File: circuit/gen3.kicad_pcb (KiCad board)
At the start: 2 copper layers, 100 x 88.9 mm, 43 parts, among them J1 Jack-DC, J2 Conn_02x20_Row_Letter_Last, J3 Conn_02x20_Row_Letter_Last, J4 Conn_01x02_Socket, Q1 2SC1815, Q2 2SC1815, Q3 2SC1815, Q4 2SC1815, Q5 2SC1815, SW1 SW_Wuerth_450301014042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

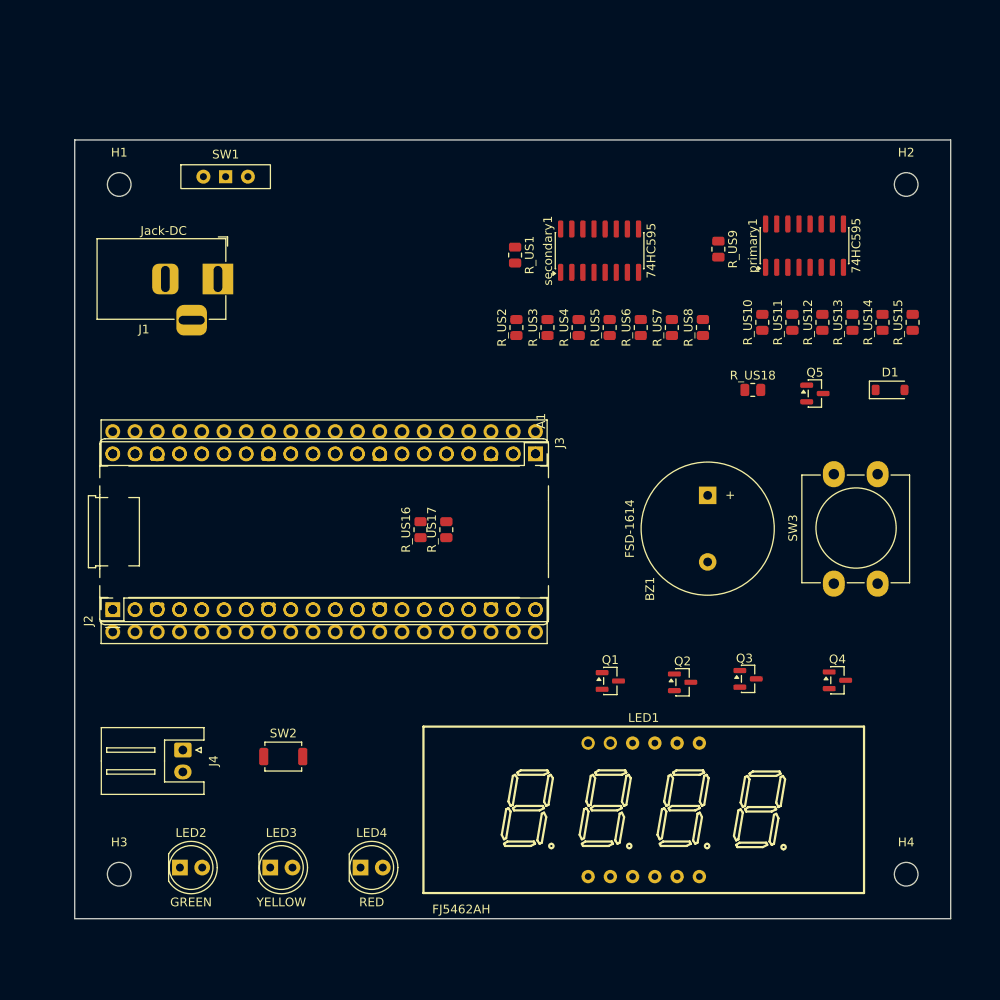
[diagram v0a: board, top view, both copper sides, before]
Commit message: [update] print pin number as footprint
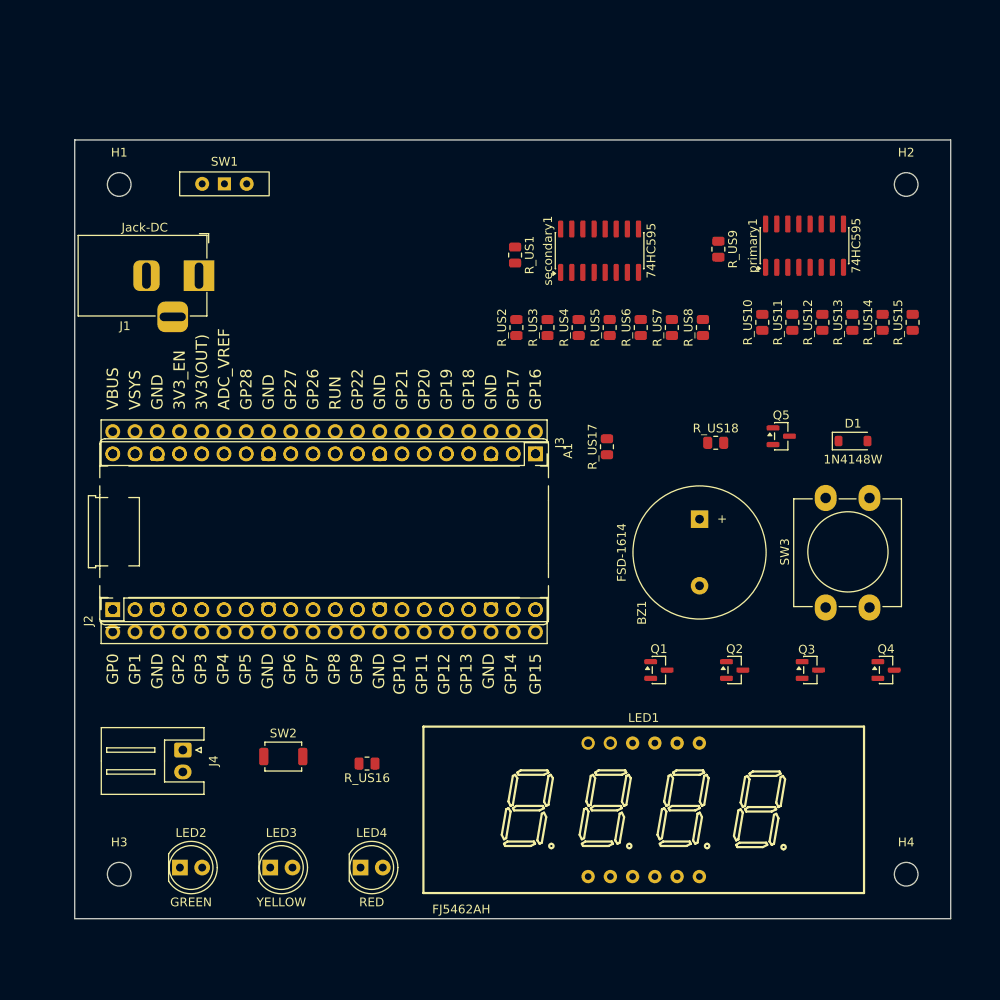
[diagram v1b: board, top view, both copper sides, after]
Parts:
- moved R_US16 27.4 mm to (119.8, 125.1), turned to 180 degrees
- moved R_US17 20.6 mm to (147.2, 89.0)
- moved R_US18 7.37 mm to (159.6, 88.5)
- moved D1 7.21 mm to (175.3, 88.3)
- moved Q3 7.18 mm to (170.4, 114.5)
- moved Q5 6.21 mm to (167.1, 87.8)
- moved Q2 6.11 mm to (161.7, 114.5)
- moved Q1 5.69 mm to (153.1, 114.5)
- moved Q4 5.67 mm to (179.0, 114.5)
- moved SW3 2.87 mm to (172.1, 107.3)
- moved BZ1 2.87 mm to (157.7, 97.2)
- moved J1 2.19 mm to (100.6, 69.4)
- moved SW1 0.83 mm to (103.5, 59.0)

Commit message: [update] add the regulation as footprint to back side
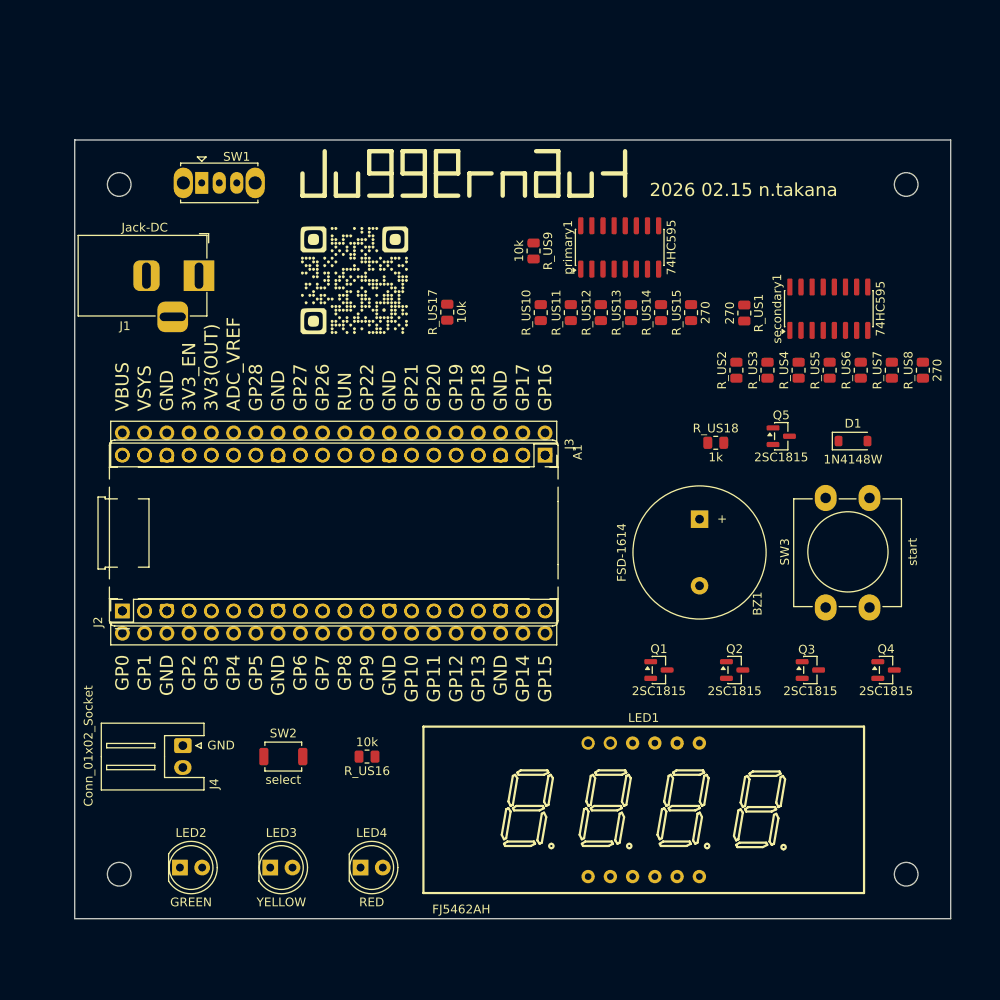
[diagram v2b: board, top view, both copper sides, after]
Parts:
- added G***: LOGO, Library:QR_juggernaut, F.Cu at (118.3, 70.0)
- SW1: footprint Button_Switch_THT:SW_Slide-03_Wuerth-WS-SLTV_10x2.5x6.4_P2.54mm -> Button_Switch_THT:SW_Slide_SPDT_Straight_CK_OS102011MS2Q
- moved R_US1 27.0 mm to (162.8, 73.7)
- moved secondary1 27.0 mm to (172.5, 73.2)
- moved R_US3 25.6 mm to (165.5, 80.2)
- moved R_US5 25.6 mm to (172.6, 80.2)
- moved R_US7 25.6 mm to (179.7, 80.2)
- moved R_US8 25.6 mm to (183.2, 80.2)
- moved R_US2 25.6 mm to (161.9, 80.2)
- moved R_US4 25.6 mm to (169.0, 80.2)
- moved R_US6 25.6 mm to (176.1, 80.2)
- moved R_US13 25.3 mm to (149.9, 73.7)
- moved R_US15 25.3 mm to (156.8, 73.7)
- moved R_US10 25.3 mm to (139.6, 73.7)
- moved R_US11 25.3 mm to (143.0, 73.7)
- moved R_US12 25.3 mm to (146.5, 73.7)
- moved R_US14 25.3 mm to (153.3, 73.7)
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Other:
- board text added: "2026 02.15 n.takana"
- board text added: "A. 総則 本競技は運営，出題者，挑戦者の3つの立場で構成される． 装置を用意する側をgiver（出題者），装置を解除する側をsolver（挑戦者）と呼ぶ． 装置に取り付けられたタイマー残り時間が0になる前にプログラムで決められた状態になった場合succeeded（または解除）となる． 装置に取り付けられたタイマー残り時間が0でない競技中の状態をin-process（または解除中）という． 装置に取り付けられたタイマー残り時間が0になる，もしくはプログラムで定められた手順から外れた状態になった場合failed（または解除失敗）となる． 競技は装置に取り付けられたボタンを押下することで始まり，succeeded/failedのいずれかで終了する． 禁止事項（後述の競技規則C項7条，D項3条）に抵触した参加書は最終結果から除外される． 複数のgiverが勝敗を争う場合，原則以下のように決定す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"

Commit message: [update] update layout to allocate enough connector placing space
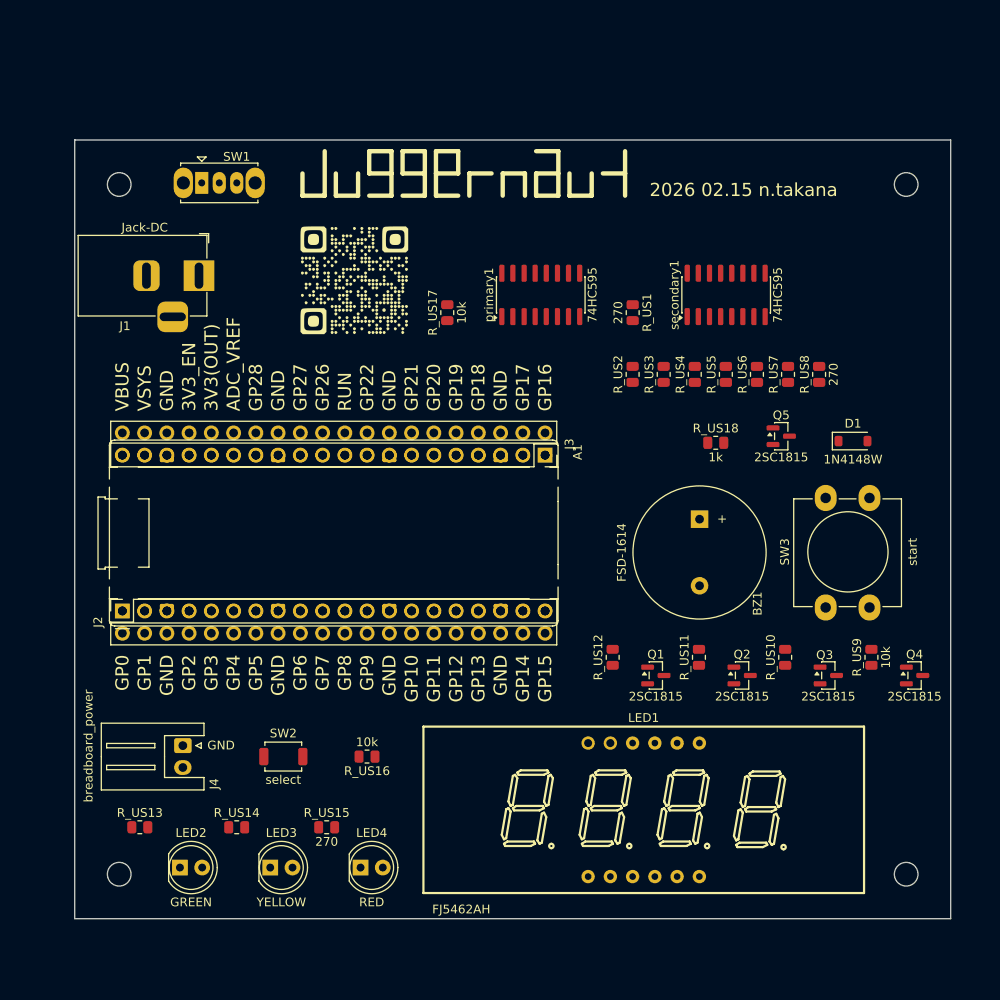
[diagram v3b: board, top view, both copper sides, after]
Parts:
- J4: value Conn_01x02_Socket -> breadboard_power
- moved R_US13 81.2 mm to (93.8, 132.4), turned to 0 degrees
- moved R_US14 76.1 mm to (104.9, 132.4), turned to 0 degrees
- moved R_US15 72.0 mm to (115.2, 132.4), turned to 0 degrees
- moved R_US9 60.3 mm to (177.4, 113.0), turned to 90 degrees
- moved R_US10 48.2 mm to (167.5, 113.0)
- moved R_US11 42.0 mm to (157.7, 113.0)
- moved R_US12 39.4 mm to (147.8, 113.0)
- moved R_US1 12.7 mm to (150.1, 73.7)
- moved R_US8 11.9 mm to (171.4, 80.7)
- moved R_US2 11.9 mm to (150.1, 80.7)
- moved R_US3 11.9 mm to (153.6, 80.7)
- moved R_US4 11.9 mm to (157.2, 80.7)
- moved R_US5 11.9 mm to (160.7, 80.7)
- moved R_US6 11.9 mm to (164.3, 80.7)
- moved R_US7 11.9 mm to (167.8, 80.7)
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
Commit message: [add] add connector for detonator
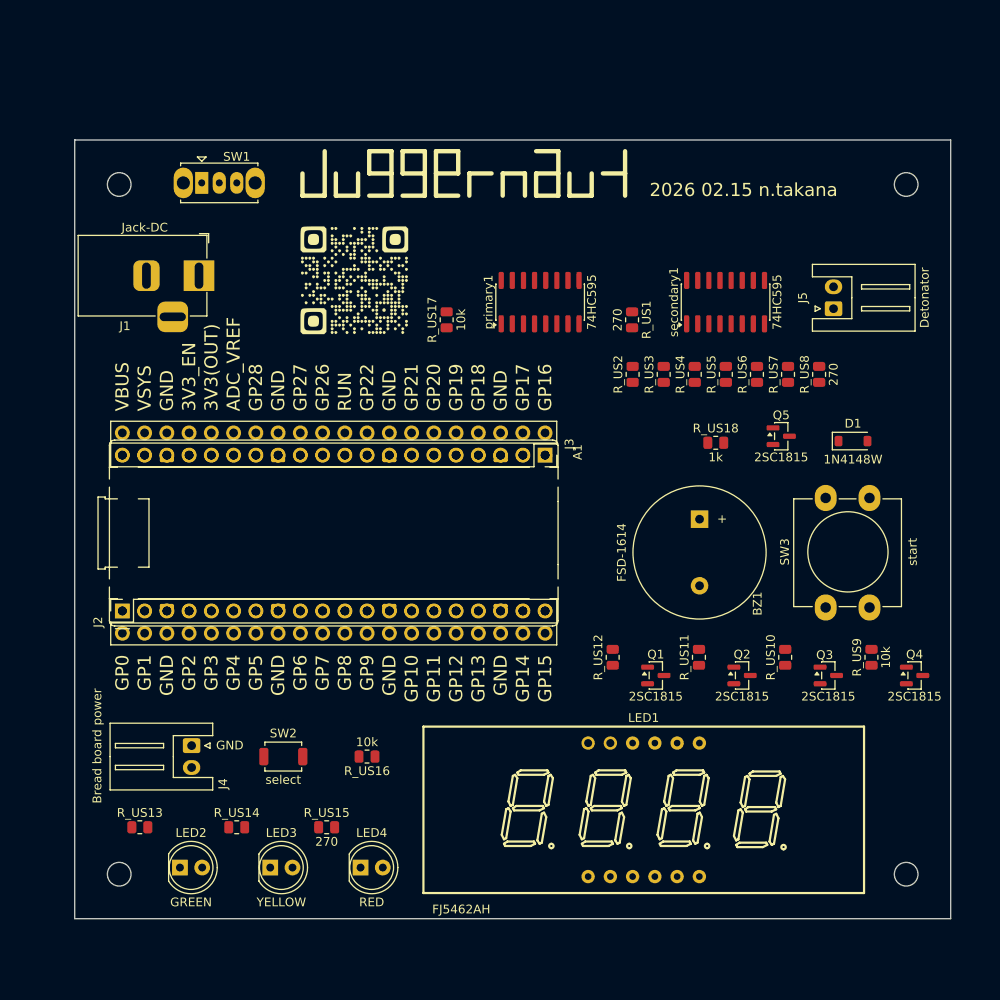
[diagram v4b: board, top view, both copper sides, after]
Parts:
- added J5: Detonator, Connector_JST:JST_XH_S2B-XH-A_1x02_P2.50mm_Horizontal, F.Cu at (173.0, 73.2)
- J4: value breadboard_power -> Bread board power
- moved J4 1.00 mm to (99.8, 123.1)
- moved R_US1 0.82 mm to (150.0, 74.5)
- moved R_US17 0.82 mm to (128.9, 74.5)
- moved primary1 0.82 mm to (139.5, 72.5)
- moved secondary1 0.82 mm to (160.7, 72.5)
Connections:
- R_US16 pad 1: /Pin23 -> /Pin24
- SW2 pad 2: /Pin23 -> /Pin24
- primary1 pad 11: /Pin24 -> /Pin25
- primary1 pad 12: /Pin25 -> /Pin26
- primary1 pad 14: /Pin26 -> /Pin27
- secondary1 pad 11: /Pin24 -> /Pin25
- secondary1 pad 12: /Pin25 -> /Pin26

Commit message: [fix] update slide switch's footprint
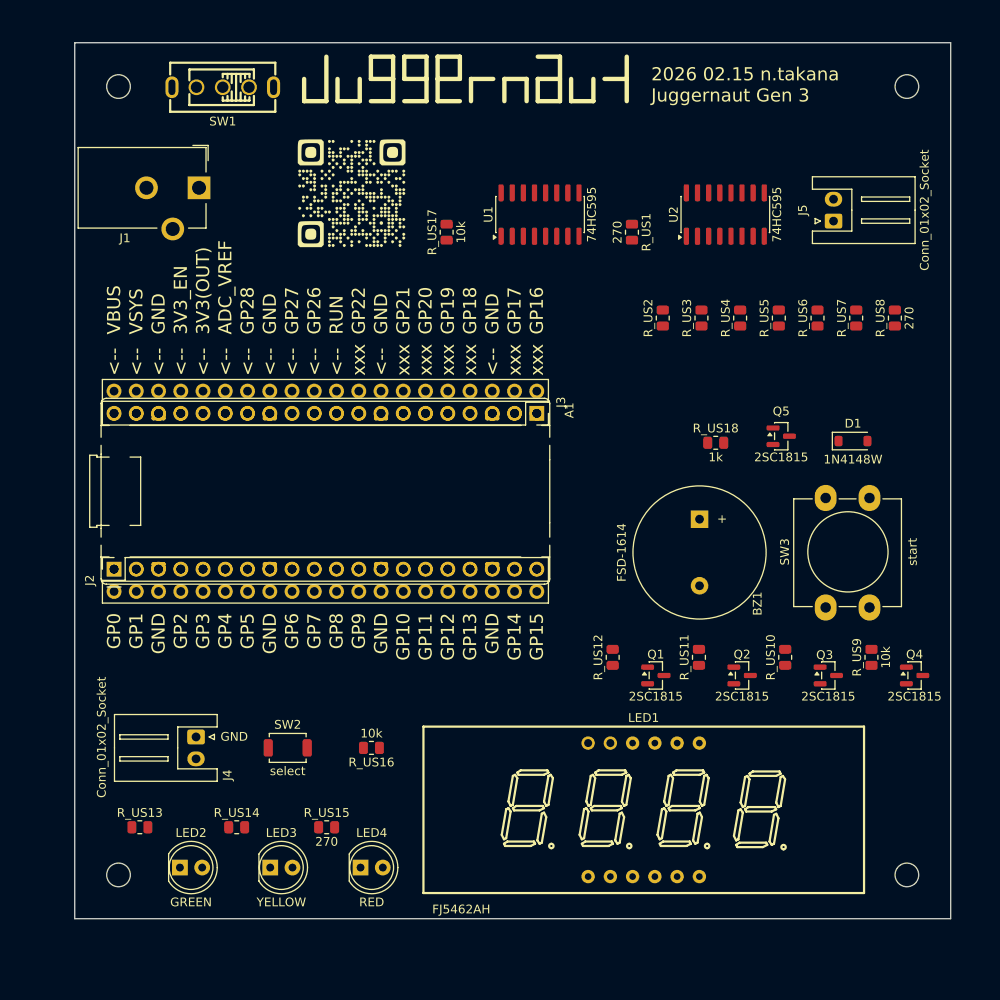
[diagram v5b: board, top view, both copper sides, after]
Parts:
- removed primary1, secondary1: 74HC595, Package_SO:SOIC-16_3.9x9.9mm_P1.27mm
- added U1: 74HC595, Package_SO:SOIC-16_3.9x9.9mm_P1.27mm, F.Cu at (139.5, 62.5)
- added U2: 74HC595, Package_SO:SOIC-16_3.9x9.9mm_P1.27mm, F.Cu at (160.7, 62.5)
- J1: footprint Connector_BarrelJack:BarrelJack_Horizontal -> Connector_BarrelJack:BarrelJack_CUI_PJ-102AH_Horizontal
- J4: value Bread board power -> Conn_01x02_Socket
- J5: value Detonator -> Conn_01x02_Socket
- SW1: footprint Button_Switch_THT:SW_Slide_SPDT_Straight_CK_OS102011MS2Q -> MyParts:SW-TH_SS-12F44-G5
- moved SW1 11.2 mm to (103.3, 47.9), turned to 180 degrees
- moved H1 11.2 mm to (91.4, 47.9)
- moved H2 11.2 mm to (181.4, 47.9)
- moved R_US8 10.8 mm to (180.0, 74.3)
- moved R_US7 10.1 mm to (175.6, 74.3)
- moved J1 10.0 mm to (100.6, 59.4), turned to -90 degrees
- moved R_US1 10.0 mm to (150.0, 64.5)
- moved R_US17 10.0 mm to (128.9, 64.5)
- moved J5 10.00 mm to (173.0, 63.2)
- moved G*** 9.94 mm to (118.0, 60.0)
- moved R_US6 9.44 mm to (171.2, 74.3)
- moved R_US5 8.83 mm to (166.8, 74.3)
- moved R_US4 8.25 mm to (162.4, 74.3)
- moved R_US3 7.74 mm to (158.0, 74.3)
- moved R_US2 7.29 mm to (153.5, 74.3)
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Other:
- board size 100 x 88.9 mm -> 100 x 100 mm
- board text added: "2026 02.15 n.takana Juggernaut Gen 3"
- board text removed: "2026 02.15 n.takana"

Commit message: [wip][add] apply auto generated routing
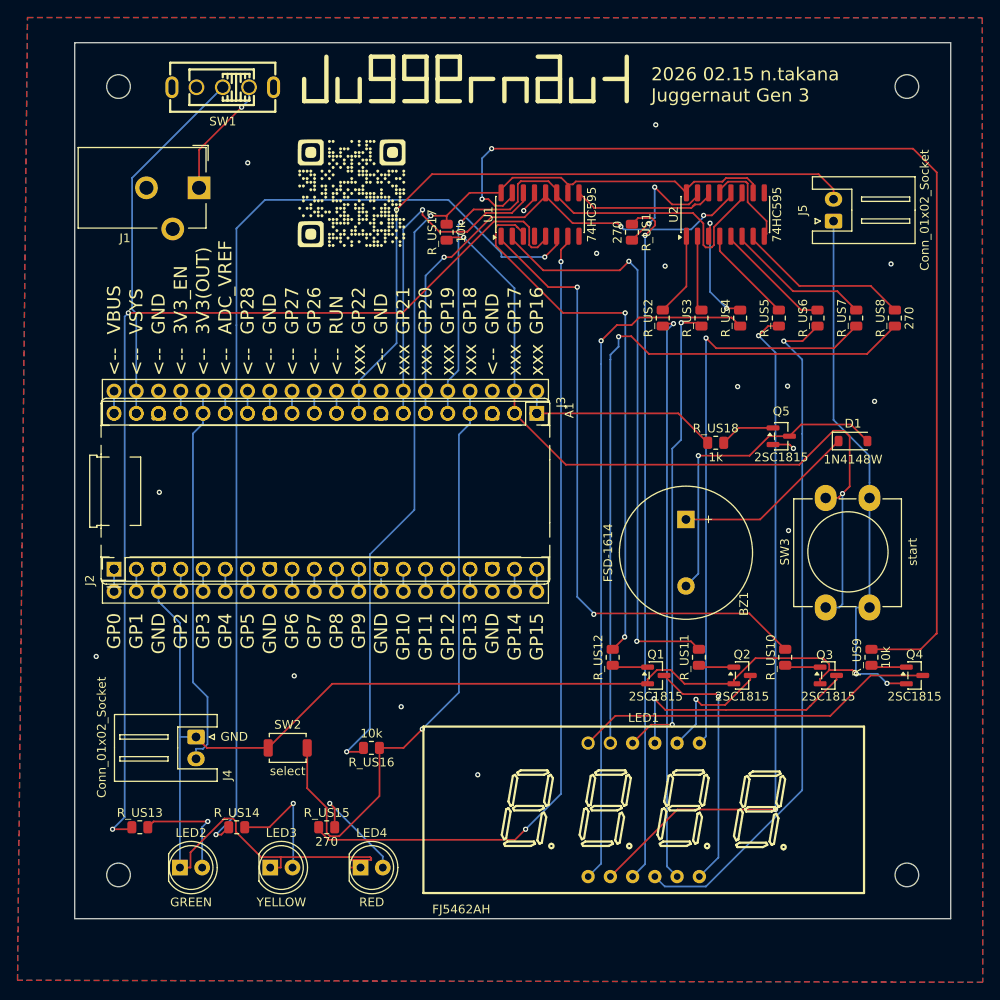
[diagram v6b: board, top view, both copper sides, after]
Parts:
- moved BZ1 1.55 mm to (156.2, 97.3)
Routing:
- net GNDPWR: track 0.00 -> 234.5 mm, vias 0 -> 18
- net Net-(U1-QA): track 0.00 -> 123.6 mm, vias 0 -> 2
- net Net-(U1-QF): track 0.00 -> 117.1 mm, vias 0 -> 2
- net Net-(U1-QG): track 0.00 -> 114.4 mm, vias 0 -> 2
- net +3V3: track 0.00 -> 111.1 mm, vias 0 -> 2
- net Net-(U1-QH): track 0.00 -> 94.6 mm, vias 0 -> 2
- net /Pin22: track 0.00 -> 90.9 mm, vias 0 -> 2
- net /7seg_led/A: track 0.00 -> 80.5 mm, vias 0 -> 1
- net /7seg_led/D: track 0.00 -> 79.7 mm, vias 0 -> 2
- net /7seg_led/E: track 0.00 -> 79.2 mm, vias 0 -> 1
- net /7seg_led/DP: track 0.00 -> 79.0 mm, vias 0 -> 1
- net /7seg_led/C: track 0.00 -> 78.5 mm, vias 0 -> 1
- net /Pin29: track 0.00 -> 78.5 mm, vias 0 -> 1
- net Net-(U1-QB): track 0.00 -> 73.1 mm, vias 0 -> 2
- net /Pin24: track 0.00 -> 70.8 mm, vias 0 -> 1
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- added copper zone on B.Cu, net GNDPWR
- added copper zone on F.Cu, net GNDPWR

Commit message: [add] add the GND zone
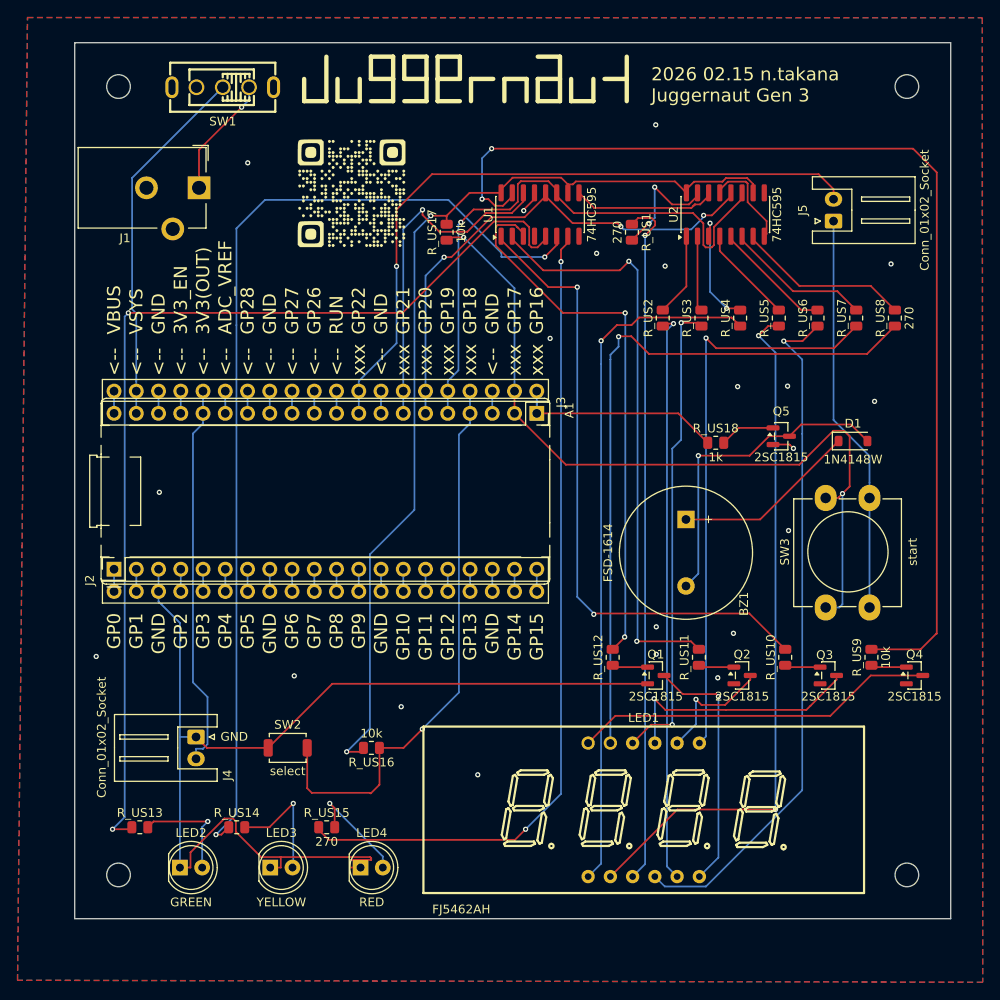
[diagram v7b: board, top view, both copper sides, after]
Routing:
- net GNDPWR: track 234.5 -> 189.1 mm, vias 18 -> 21
- net /Pin24: track 70.8 -> 64.3 mm
- net /Pin8: track 0.00 -> 2.54 mm
- net /Pin38: track 0.00 -> 2.54 mm
- net /Pin28: track 0.00 -> 2.54 mm
- net /Pin23: track 0.00 -> 2.54 mm
- net /Pin18: track 0.00 -> 2.54 mm
- net /Pin21: track 23.5 -> 24.8 mm
- net /Pin13: track 1.44 -> 2.54 mm
